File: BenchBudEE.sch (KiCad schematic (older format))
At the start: 0 parts

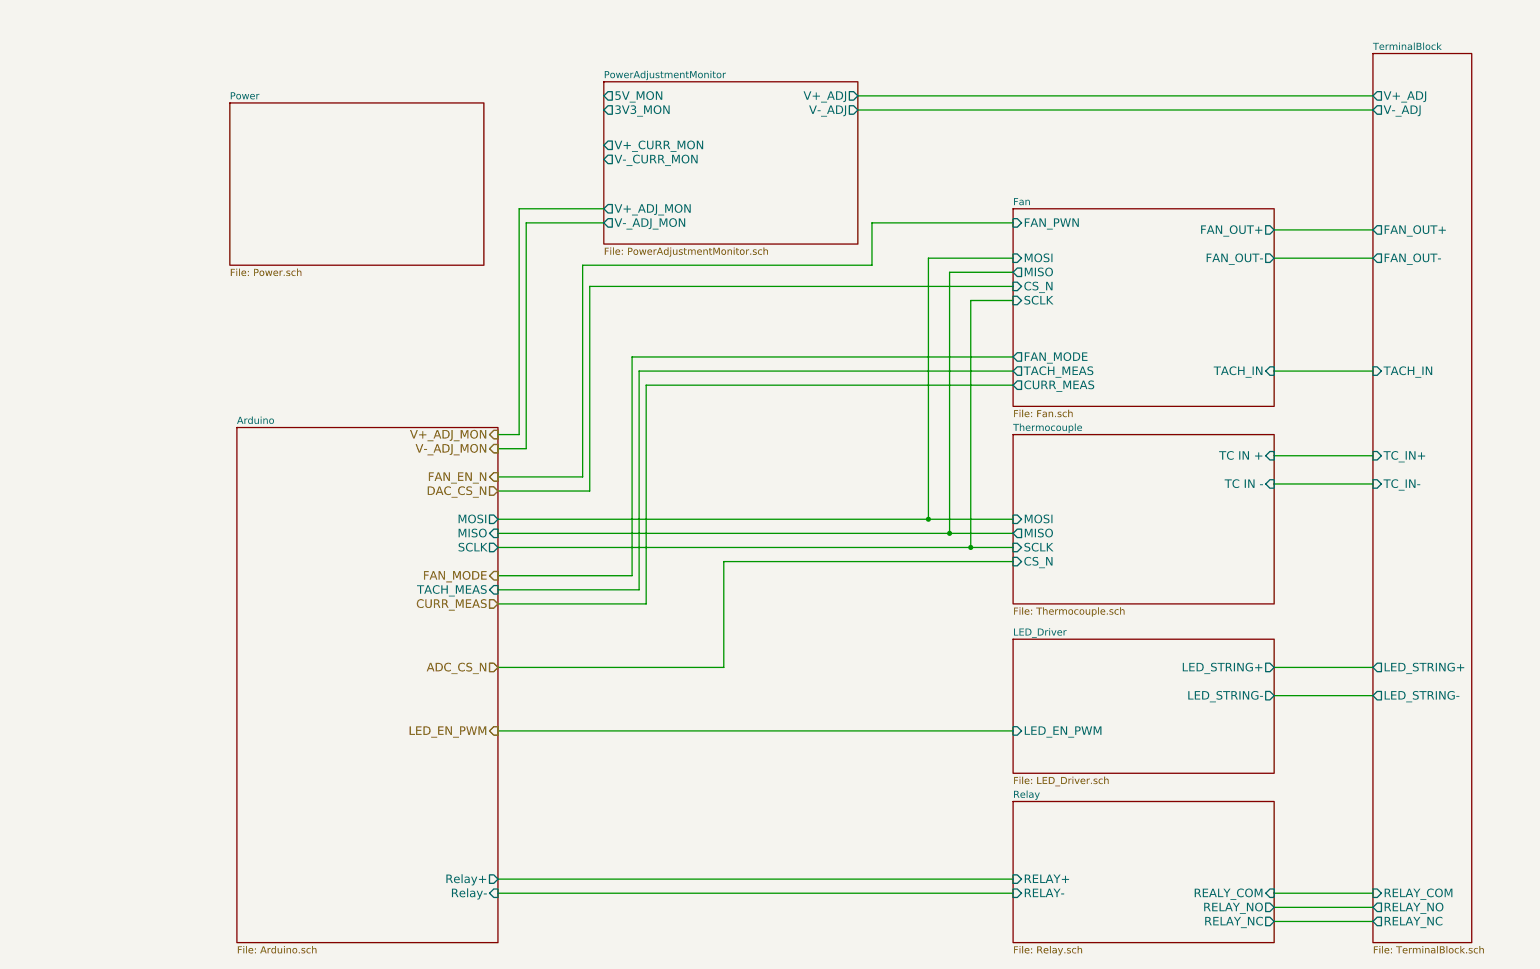
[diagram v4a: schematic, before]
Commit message: 5.4 Video 1/2 Associating and Placing the Thermocouple Module
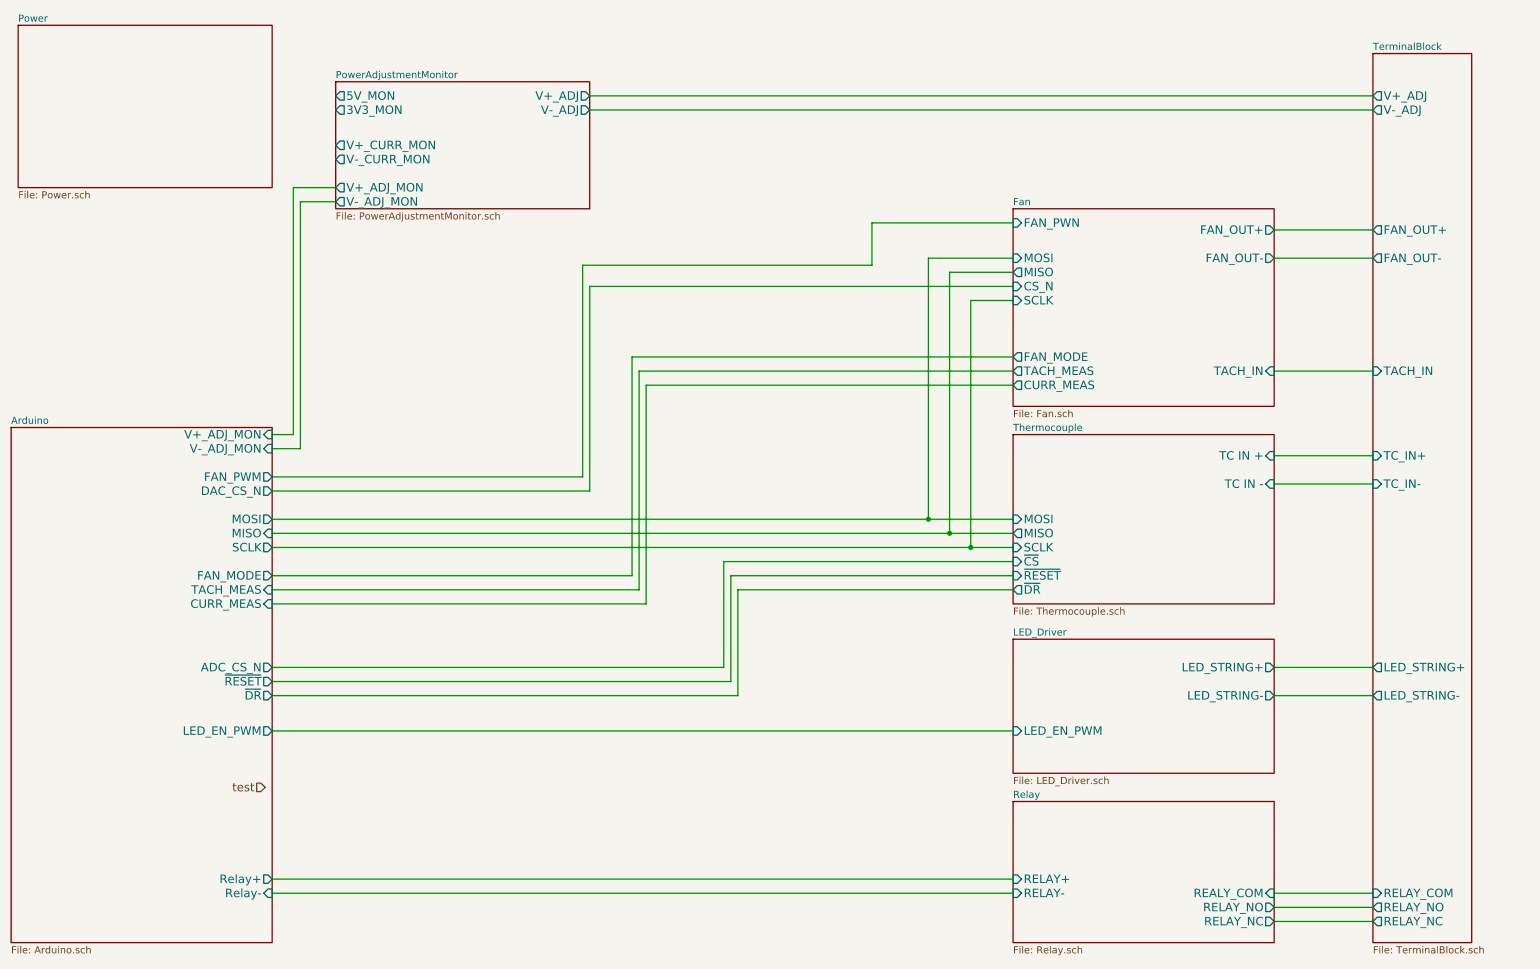
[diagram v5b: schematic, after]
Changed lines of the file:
@@
 Sheet 1 9
 Title ""
-Date "19 feb 2014"
+Date "21 feb 2014"
 Rev ""
 Comp ""
@@
 $EndSheet
 $Sheet
-S 2050 1150 1800 1150
+S 550  600  1800 1150
 U 52EBE800
 F0 "Power" 50
@@
 $EndSheet
 $Sheet
-S 4700 1000 1800 1150
-U 52F44BE7
-F0 "PowerAdjustmentMonitor" 50
-F1 "PowerAdjustmentMonitor.sch" 50
-F2 "V-_ADJ" O R 6500 1200 60
-F3 "3V3_MON" O L 4700 1200 60
-F4 "V+_ADJ_MON" O L 4700 1900 60
-F5 "V-_ADJ_MON" O L 4700 2000 60
-F6 "V+_CURR_MON" O L 4700 1450 60
-F7 "V-_CURR_MON" O L 4700 1550 60
-F8 "V+_ADJ" O R 6500 1100 60
-F9 "5V_MON" O L 4700 1100 60
-$EndSheet
-$Sheet
 S 7600 1900 1850 1400
 U 52EBE84E
@@
 $EndSheet
 Wire Wire Line
-	10150 1100 6500 1100
-Wire Wire Line
-	6500 1200 10150 1200
+	10150 1100 4600 1100
+Wire Wire Line
+	4600 1200 10150 1200
 Wire Wire Line
 	9450 2050 10150 2050
@@
 Wire Wire Line
 	9450 6950 10150 6950
-Text HLabel 3950 3500 0    60   Output ~ 0
-V+_ADJ_MON
-Text HLabel 3950 3600 0    60   Output ~ 0
-V-_ADJ_MON
-Text HLabel 3950 3800 0    60   Output ~ 0
-FAN_EN_N
-Text HLabel 3950 3900 0    60   Input ~ 0
-DAC_CS_N
-Text HLabel 3950 4700 0    60   Input ~ 0
-CURR_MEAS
-Text HLabel 3950 5150 0    60   Input ~ 0
-ADC_CS_N
-Text HLabel 3950 5600 0    60   Output ~ 0
-LED_EN_PWM
-Wire Wire Line
-	3950 6650 7600 6650
-Wire Wire Line
-	3950 6750 7600 6750
+Wire Wire Line
+	2350 6650 7600 6650
+Wire Wire Line
+	2350 6750 7600 6750
+Wire Wire Line
+	2350 3500 2500 3500
+Wire Wire Line
+	2500 3500 2500 1750
+Wire Wire Line
+	2500 1750 2800 1750
+Wire Wire Line
+	2800 1850 2550 1850
+Wire Wire Line
+	2550 1850 2550 3600
+Wire Wire Line
+	2550 3600 2350 3600
+Wire Wire Line
+	6600 2000 7600 2000
+Wire Wire Line
+	2350 3800 4550 3800
+Wire Wire Line
+	4550 3800 4550 2300
+Wire Wire Line
+	4550 2300 6600 2300
+Wire Wire Line
+	6600 2300 6600 2000
+Wire Wire Line
+	2350 3900 4600 3900
+Wire Wire Line
+	4600 3900 4600 2450
+Wire Wire Line
+	4600 2450 7600 2450
+$Sheet
+S 500  3450 1850 3650
+U 52EBE680
+F0 "Arduino" 50
+F1 "Arduino.sch" 50
+F2 "Relay+" O R 2350 6650 60
+F3 "Relay-" I R 2350 6750 60
+F4 "MOSI" O R 2350 4100 60
+F5 "MISO" I R 2350 4200 60
+F6 "SCLK" O R 2350 4300 60
+F7 "TACH_MEAS" I R 2350 4600 60
+F8 "ADC_CS_N" O R 2350 5150 60
+F9 "FAN_PWM" O R 2350 3800 60
+F10 "V-_ADJ_MON" I R 2350 3600 60
+F11 "CURR_MEAS" I R 2350 4700 60
+F12 "DAC_CS_N" O R 2350 3900 60
+F13 "LED_EN_PWM" O R 2350 5600 60
+F14 "~DR" O R 2350 5350 60
+F15 "~RESET" O R 2350 5250 60
+F16 "V+_ADJ_MON" I R 2350 3500 60
+F17 "FAN_MODE" O R 2350 4500 60
+$EndSheet
+Wire Wire Line
+	2350 4600 4950 4600
+Wire Wire Line
+	4950 4600 4950 3050
+Wire Wire Line
+	4950 3050 7600 3050
+Wire Wire Line
+	2350 4700 5000 4700
+Wire Wire Line
+	5000 4700 5000 3150
+Wire Wire Line
+	5000 3150 7600 3150
+Wire Wire Line
+	5550 5150 2350 5150
+Wire Wire Line
+	2350 5600 7600 5600
+Wire Wire Line
+	2350 4100 7600 4100
+Wire Wire Line
+	2350 4200 7600 4200
+Wire Wire Line
+	2350 4300 7600 4300
+Wire Wire Line
+	5550 5150 5550 4400
+Wire Wire Line
+	5550 4400 7600 4400
+Wire Wire Line
+	7600 2250 7000 2250
+Wire Wire Line
+	7000 2250 7000 4100
+Connection ~ 7000 4100
+Wire Wire Line
+	7600 2350 7150 2350
+Wire Wire Line
+	7150 2350 7150 4200
+Connection ~ 7150 4200
+Wire Wire Line
+	7600 2550 7300 2550
+Wire Wire Line
+	7300 2550 7300 4300
+Connection ~ 7300 4300
+Wire Wire Line
+	7600 2950 4900 2950
+Wire Wire Line
+	4900 2950 4900 4500
+Wire Wire Line
+	4900 4500 2350 4500
+$Sheet
+S 2800 1000 1800 900
+U 52F44BE7
+F0 "PowerAdjustmentMonitor" 50
+F1 "PowerAdjustmentMonitor.sch" 50
+F2 "V-_ADJ" O R 4600 1200 60
+F3 "3V3_MON" O L 2800 1200 60
+F4 "V+_ADJ_MON" O L 2800 1750 60
+F5 "V-_ADJ_MON" O L 2800 1850 60
+F6 "V+_CURR_MON" O L 2800 1450 60
+F7 "V-_CURR_MON" O L 2800 1550 60
+F8 "V+_ADJ" O R 4600 1100 60
+F9 "5V_MON" O L 2800 1100 60
+$EndSheet
 $Sheet
 S 7600 3500 1850 1200
@@
 F5 "MISO" O L 7600 4200 60
 F6 "SCLK" I L 7600 4300 60
-F7 "CS_N" I L 7600 4400 60
-$EndSheet
-Wire Wire Line
-	3950 3500 4100 3500
-Wire Wire Line
-	4100 3500 4100 1900
-Wire Wire Line
-	4100 1900 4700 1900
-Wire Wire Line
-	4700 2000 4150 2000
-Wire Wire Line
-	4150 2000 4150 3600
-Wire Wire Line
-	4150 3600 3950 3600
-Wire Wire Line
-	6600 2000 7600 2000
-Wire Wire Line
-	3950 3800 4550 3800
-Wire Wire Line
-	4550 3800 4550 2300
-Wire Wire Line
-	4550 2300 6600 2300
-Wire Wire Line
-	6600 2300 6600 2000
-Wire Wire Line
-	3950 3900 4600 3900
-Wire Wire Line
-	4600 3900 4600 2450
-Wire Wire Line
-	4600 2450 7600 2450
-$Sheet
-S 2100 3450 1850 3650
-U 52EBE680
-F0 "Arduino" 50
-F1 "Arduino.sch" 50
-F2 "Relay+" O R 3950 6650 60
-F3 "Relay-" I R 3950 6750 60
-F4 "MOSI" O R 3950 4100 60
-F5 "MISO" I R 3950 4200 60
-F6 "SCLK" O R 3950 4300 60
-F7 "TACH_MEAS" I R 3950 4600 60
-$EndSheet
-Wire Wire Line
-	3950 4600 4950 4600
-Wire Wire Line
-	4950 4600 4950 3050
-Wire Wire Line
-	4950 3050 7600 3050
-Wire Wire Line
-	3950 4700 5000 4700
-Wire Wire Line
-	5000 4700 5000 3150
-Wire Wire Line
-	5000 3150 7600 3150
-Wire Wire Line
-	5550 5150 3950 5150
-Wire Wire Line
-	3950 5600 7600 5600
-Wire Wire Line
-	3950 4100 7600 4100
-Wire Wire Line
-	3950 4200 7600 4200
-Wire Wire Line
-	3950 4300 7600 4300
-Wire Wire Line
-	5550 5150 5550 4400
-Wire Wire Line
-	5550 4400 7600 4400
-Wire Wire Line
-	7600 2250 7000 2250
-Wire Wire Line
-	7000 2250 7000 4100
-Connection ~ 7000 4100
-Wire Wire Line
-	7600 2350 7150 2350
-Wire Wire Line
-	7150 2350 7150 4200
-Connection ~ 7150 4200
-Wire Wire Line
-	7600 2550 7300 2550
-Wire Wire Line
-	7300 2550 7300 4300
-Connection ~ 7300 4300
-Wire Wire Line
-	7600 2950 4900 2950
-Wire Wire Line
-	4900 2950 4900 4500
-Wire Wire Line
-	4900 4500 3950 4500
-Text HLabel 3950 4500 0    60   Output ~ 0
-FAN_MODE
+F7 "~CS" I L 7600 4400 60
+F8 "~DR" O L 7600 4600 60
+F9 "~RESET" I L 7600 4500 60
+$EndSheet
+Text HLabel 2300 6000 0    60   Input ~ 0
+test
+Wire Wire Line
+	2350 5250 5600 5250
+Wire Wire Line
+	5600 5250 5600 4500
+Wire Wire Line
+	5600 4500 7600 4500
+Wire Wire Line
+	7600 4600 5650 4600
+Wire Wire Line
+	5650 4600 5650 5350
+Wire Wire Line
+	5650 5350 2350 5350
 $EndSCHEMATC

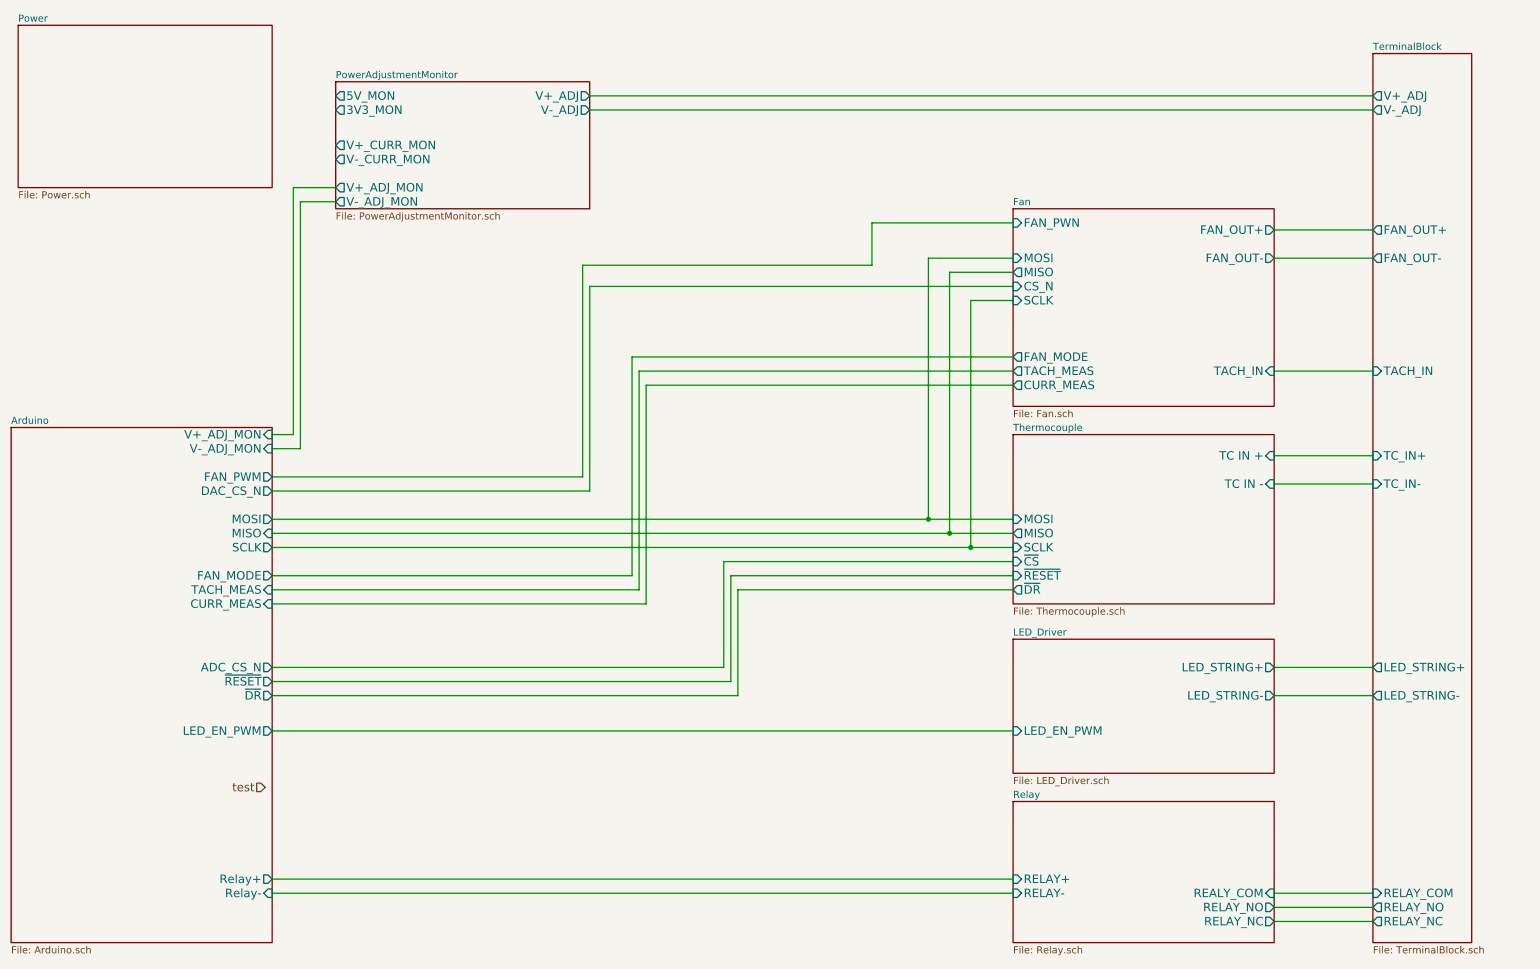
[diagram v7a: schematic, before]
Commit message: 5.7 Video 1/2 Associating and Placing the Arduino Module
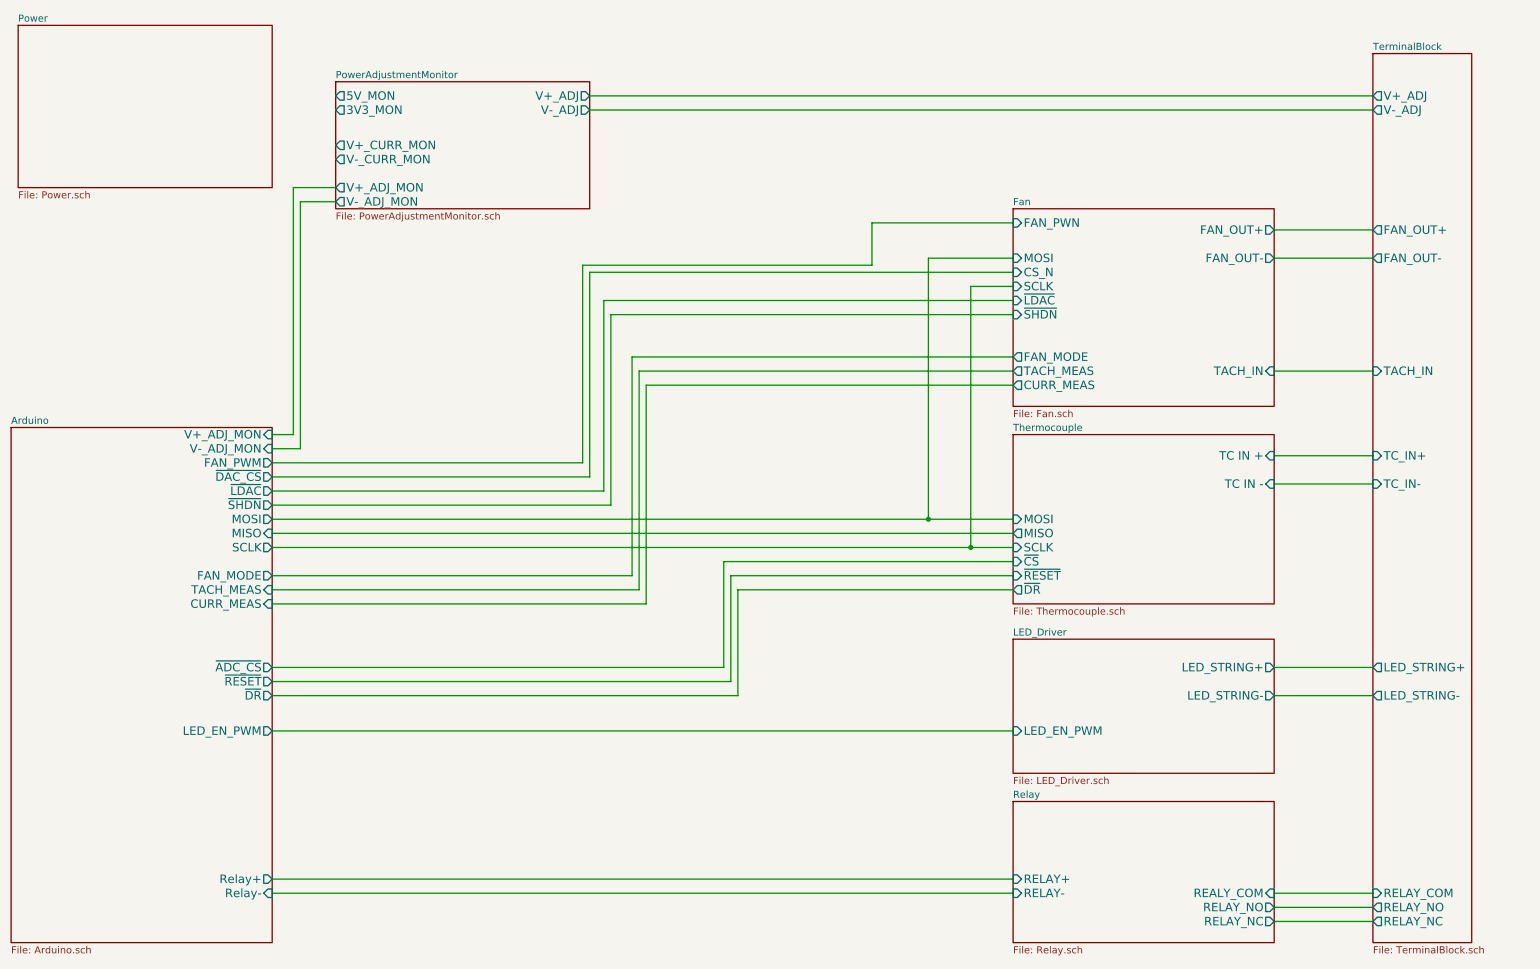
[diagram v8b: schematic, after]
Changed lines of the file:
@@
 Sheet 1 9
 Title ""
-Date "22 feb 2014"
+Date "23 feb 2014"
 Rev ""
 Comp ""
@@
 F3 "FAN_OUT-" O R 9450 2250 60
 F4 "MOSI" I L 7600 2250 60
-F5 "MISO" O L 7600 2350 60
-F6 "CS_N" I L 7600 2450 60
-F7 "SCLK" I L 7600 2550 60
-F8 "TACH_MEAS" O L 7600 3050 60
-F9 "CURR_MEAS" O L 7600 3150 60
-F10 "TACH_IN" I R 9450 3050 60
-F11 "FAN_PWN" I L 7600 2000 60
-F12 "FAN_MODE" O L 7600 2950 60
+F5 "CS_N" I L 7600 2350 60
+F6 "SCLK" I L 7600 2450 60
+F7 "TACH_MEAS" O L 7600 3050 60
+F8 "CURR_MEAS" O L 7600 3150 60
+F9 "TACH_IN" I R 9450 3050 60
+F10 "FAN_PWN" I L 7600 2000 60
+F11 "FAN_MODE" O L 7600 2950 60
+F12 "~LDAC" I L 7600 2550 60
+F13 "~SHDN" I L 7600 2650 60
 $EndSheet
 Wire Wire Line
@@
 	6600 2000 7600 2000
 Wire Wire Line
-	2350 3800 4550 3800
-Wire Wire Line
-	4550 3800 4550 2300
+	2350 3700 4550 3700
+Wire Wire Line
+	4550 3700 4550 2300
 Wire Wire Line
 	4550 2300 6600 2300
@@
 	6600 2300 6600 2000
 Wire Wire Line
-	2350 3900 4600 3900
-Wire Wire Line
-	4600 3900 4600 2450
-Wire Wire Line
-	4600 2450 7600 2450
+	2350 3800 4600 3800
+Wire Wire Line
+	4600 3800 4600 2350
+Wire Wire Line
+	4600 2350 7600 2350
 $Sheet
 S 500  3450 1850 3650
@@
 F6 "SCLK" O R 2350 4300 60
 F7 "TACH_MEAS" I R 2350 4600 60
-F8 "ADC_CS_N" O R 2350 5150 60
-F9 "FAN_PWM" O R 2350 3800 60
-F10 "V-_ADJ_MON" I R 2350 3600 60
-F11 "CURR_MEAS" I R 2350 4700 60
-F12 "DAC_CS_N" O R 2350 3900 60
-F13 "LED_EN_PWM" O R 2350 5600 60
-F14 "~DR" O R 2350 5350 60
-F15 "~RESET" O R 2350 5250 60
-F16 "V+_ADJ_MON" I R 2350 3500 60
-F17 "FAN_MODE" O R 2350 4500 60
+F8 "FAN_PWM" O R 2350 3700 60
+F9 "V-_ADJ_MON" I R 2350 3600 60
+F10 "CURR_MEAS" I R 2350 4700 60
+F11 "LED_EN_PWM" O R 2350 5600 60
+F12 "~DR" O R 2350 5350 60
+F13 "~RESET" O R 2350 5250 60
+F14 "V+_ADJ_MON" I R 2350 3500 60
+F15 "FAN_MODE" O R 2350 4500 60
+F16 "~LDAC" O R 2350 3900 60
+F17 "~SHDN" O R 2350 4000 60
+F18 "~ADC_CS" O R 2350 5150 60
+F19 "~DAC_CS" O R 2350 3800 60
 $EndSheet
 Wire Wire Line
@@
 Connection ~ 7000 4100
 Wire Wire Line
-	7600 2350 7150 2350
-Wire Wire Line
-	7150 2350 7150 4200
-Connection ~ 7150 4200
-Wire Wire Line
-	7600 2550 7300 2550
-Wire Wire Line
-	7300 2550 7300 4300
+	7600 2450 7300 2450
+Wire Wire Line
+	7300 2450 7300 4300
 Connection ~ 7300 4300
 Wire Wire Line
@@
 F9 "~RESET" I L 7600 4500 60
 $EndSheet
-Text HLabel 2300 6000 0    60   Input ~ 0
-test
 Wire Wire Line
 	2350 5250 5600 5250
@@
 Wire Wire Line
 	5650 5350 2350 5350
+Wire Wire Line
+	2350 3900 4700 3900
+Wire Wire Line
+	4700 3900 4700 2550
+Wire Wire Line
+	4700 2550 7600 2550
+Wire Wire Line
+	7600 2650 4750 2650
+Wire Wire Line
+	4750 2650 4750 4000
+Wire Wire Line
+	4750 4000 2350 4000
 $EndSCHEMATC
